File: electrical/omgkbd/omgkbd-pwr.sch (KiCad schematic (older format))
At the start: 10 parts

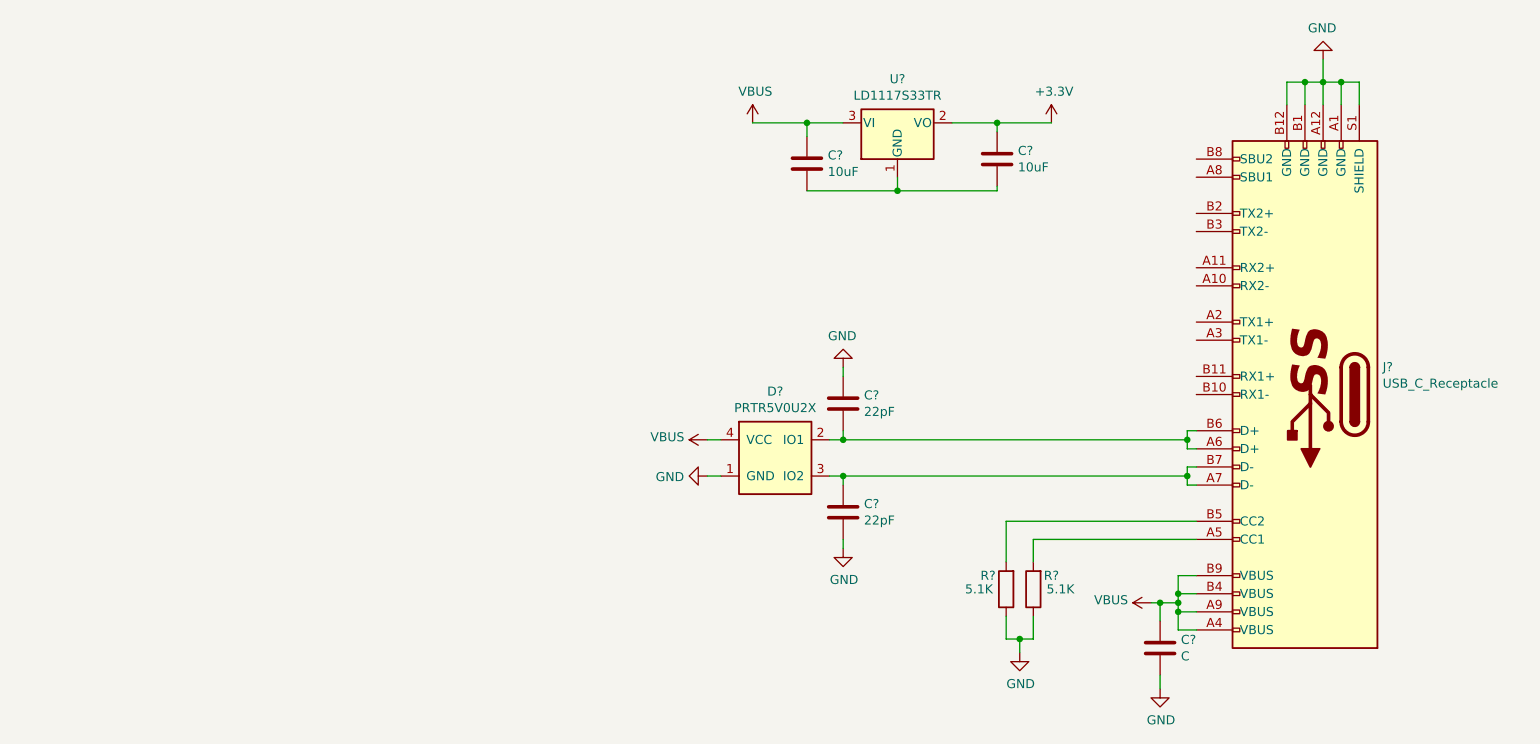
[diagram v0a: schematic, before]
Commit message: Added crystal and some capacitors
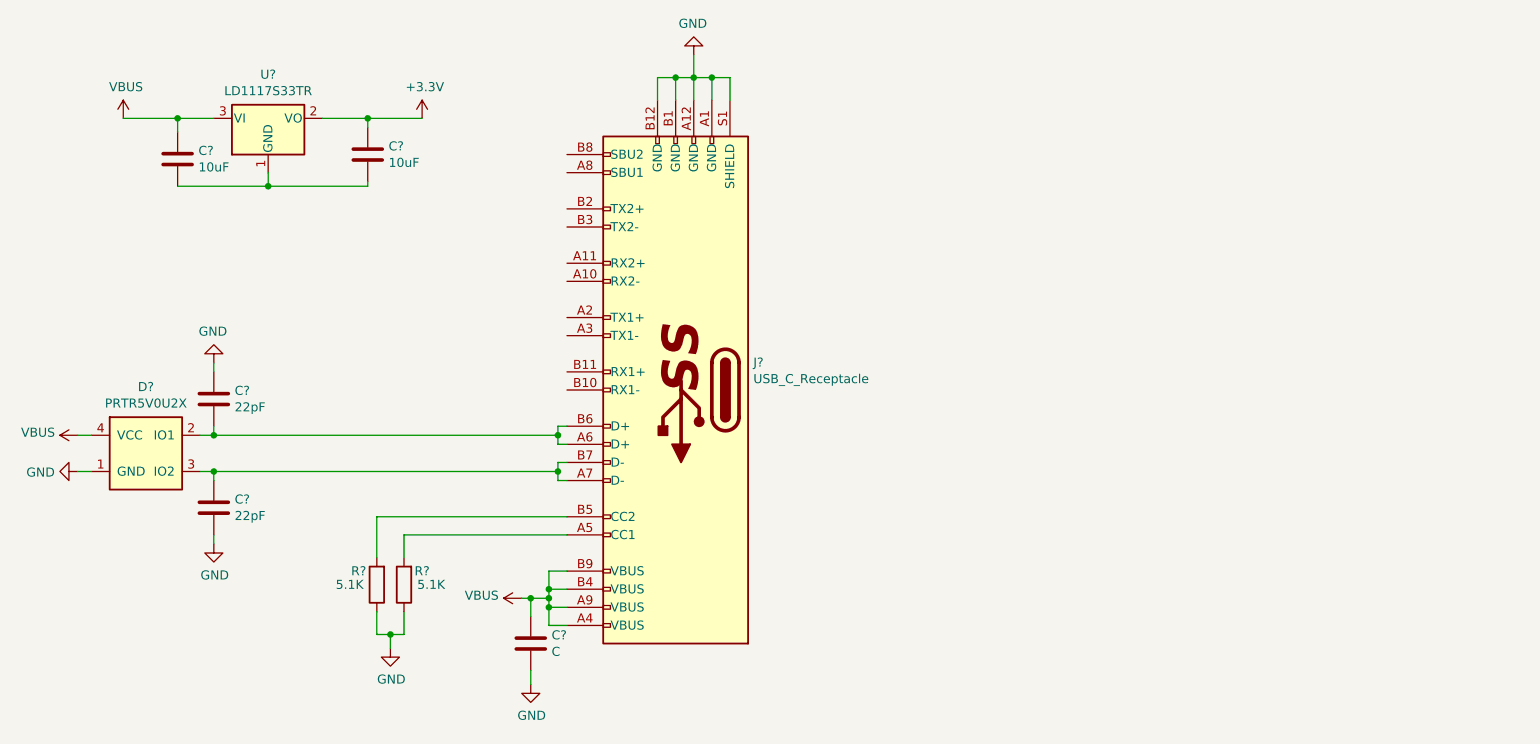
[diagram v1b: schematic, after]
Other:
- moved on the sheet: C?, D?, J?, R?, U?
